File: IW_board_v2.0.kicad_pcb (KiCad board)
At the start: 2 copper layers, 167.8 x 92.4 mm, 104 parts, among them J1 USB_C_Receptacle, J10 RIGHT WHEEL SENS, J11 STARTER CON, J12 USB_C_Receptacle, J13 USB_C_Receptacle, J14 CAN, J15 3.3V OUT, J16 5V OUT, J17 7.5V OUT, J18 OIL CON, J19 IAT CON, J2 XT90PW-M, J20 PRIM TRIGG CON, J21 SEC TRIGG CON, J22 EGT CON, J23 DATA LOGGER CON, J24 IGN CON, J25 INJ CON, J3 EMU_BLACK_A, J4 EMU_BLACK_B, J5 SAFETY, J6 INJ CON, J7 STARTER INF, J8 SERVO, J9 LEFT WHEEL SENS, K1 FINDER-34.51 INJ, K2 FINDER-34.51 STARTER, K3 FINDER-34.51 INJ, Q1 IRFP1405PBF, Q2 IRFP1405PBF, Q3 IRFP1405PBF, Q4 IRFP1405PBF, SW1 TL3342F160QG/TR, SW2 TL3342F160QG/TR, U1 AP1501_3.3, U2 AP1501_5, U3 AP1501_ADJ_7.5, U4 RP2040, U5 LM4040DBZ-3, U6 W25Q32JVSS, U7 TXS0108EPWR, U8 2EDN7524F, Y1 Crystal

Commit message: First full version of the PCB
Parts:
- J10, J23, J24, J8, J9: footprint Connector_Molex:Molex_PicoBlade_53047-0310_1x03_P1.25mm_Vertical -> TerminalBlock_Phoenix:TerminalBlock_Phoenix_MPT-0,5-3-2.54_1x03_P2.54mm_Horizontal
- J14, J15, J16, J17, J18, J19, J20, J21, J22, J25, J5, J6, J7: footprint Connector_Molex:Molex_PicoBlade_53047-0210_1x02_P1.25mm_Vertical -> TerminalBlock_Phoenix:TerminalBlock_Phoenix_MPT-0,5-2-2.54_1x02_P2.54mm_Horizontal
- moved D6 124.3 mm to (63.0, 80.7)
- moved R10 124.3 mm to (63.0, 84.0), turned to 90 degrees
- moved D1 103.6 mm to (95.1, 92.4)
- moved L1 103.6 mm to (71.5, 85.8)
- moved C4 103.6 mm to (72.2, 100.2)
- moved C7 103.6 mm to (65.2, 104.1)
- moved U1 103.6 mm to (85.1, 98.1)
- moved C1 102.5 mm to (97.2, 101.7)
- moved D2 100.7 mm to (89.2, 88.5), turned to 0 degrees
- moved R2 97.4 mm to (174.2, 121.4), turned to 0 degrees
- moved R1 95.7 mm to (170.9, 121.4), turned to 0 degrees
- moved D4 95.0 mm to (175.0, 124.0), turned to 90 degrees
- moved C3 94.2 mm to (184.3, 138.2)
- moved L3 94.2 mm to (159.7, 122.2)
- moved C6 94.2 mm to (160.4, 136.5)
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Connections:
- net Net-(R3-Pad2) renamed /CPU/D+
- net Net-(R4-Pad2) renamed /CPU/D-
- J12 pad A1: Net-(J12-PadA1) -> /IO/USB_PASSTHROUH_GND
- J12 pad A12: Net-(J12-PadA1) -> /IO/USB_PASSTHROUH_GND
- J12 pad B1: Net-(J12-PadA1) -> /IO/USB_PASSTHROUH_GND
- J12 pad B12: Net-(J12-PadA1) -> /IO/USB_PASSTHROUH_GND
- J12 pad S1: Net-(J12-PadA1) -> /IO/USB_PASSTHROUH_GND
- R8 pad 2: /CPU/GPIO25 -> /CPU/GPIO11
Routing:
- net +5V: track 0.00 -> 336.5 mm, vias 0 -> 2
- net +3.3V: track 0.00 -> 309.7 mm, vias 0 -> 4
- net GNDS: track 0.00 -> 224.3 mm
- net /IO/RS232_TXD: track 0.00 -> 183.1 mm, vias 0 -> 2
- net /IO/5V EMU: track 0.00 -> 175.9 mm, vias 0 -> 2
- net Net-(J2-PadN): track 0.00 -> 161.2 mm
- net /IO/INJ: track 0.00 -> 158.5 mm, vias 0 -> 1
- net /IO/IGN: track 0.00 -> 154.8 mm, vias 0 -> 2
- net /IO/EMU: track 0.00 -> 153.9 mm, vias 0 -> 1
- net +7.5V: track 0.00 -> 149.8 mm, vias 0 -> 2
- net /IO/IGN_COIL_#1: track 0.00 -> 129.3 mm, vias 0 -> 2
- net /IO/EGT_IN_#1: track 0.00 -> 128.6 mm
- net /PWR/7.5V: track 0.00 -> 117.8 mm, vias 0 -> 2
- net VBUS: track 0.00 -> 111.4 mm, vias 0 -> 2
- net /IO/PRIM_TRIGG: track 0.00 -> 107.4 mm
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- added copper zone on B.Cu, net GND
- added copper zone on F.Cu, net GND
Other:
- board size 167.8 x 92.4 mm -> 155.8 x 92.4 mm

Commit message: Small corrections
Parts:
- added D11: B120-E3, Diode_SMD:D_SMA, F.Cu at (87.5, 110.1)
- added F9: 7.5V 5A, FUSE_3557-2:FUSE_3557-2, F.Cu at (110.2, 125.7)
- added J26: MAP, TerminalBlock_Phoenix:TerminalBlock_Phoenix_MPT-0,5-2-2.54_1x02_P2.54mm_Horizontal, F.Cu at (215.3, 90.5)
- added J27: CLT CON, TerminalBlock_Phoenix:TerminalBlock_Phoenix_MPT-0,5-2-2.54_1x02_P2.54mm_Horizontal, F.Cu at (147.6, 70.0)
- added R17: 330, Resistor_SMD:R_0603_1608Metric, F.Cu at (148.9, 75.3)
- D10, D9: value ES1J -> SS14; footprint ES1J:DIO_ES1J -> Diode_SMD:D_SMA
- D2, D3, D4: footprint Diode_SMD:D_0603_1608Metric -> Diode_SMD:D_SMA
- J3: footprint Connector_PinHeader_2.54mm:PinHeader_2x20_P2.54mm_Vertical -> Connector_IDC:IDC-Header_2x20_P2.54mm_Vertical
- J4: footprint Connector_PinHeader_2.54mm:PinHeader_2x12_P2.54mm_Vertical -> Connector_IDC:IDC-Header_2x12_P2.54mm_Vertical
- J6: value INJ CON -> INJ_&_STARTER
- J7: value STARTER INF -> 16V OUT
- R14: value 1k -> 10k
- moved K2 29.6 mm to (199.4, 110.0)
- moved K3 22.7 mm to (199.4, 87.0)
- moved D10 20.6 mm to (201.0, 103.0), turned to 180 degrees
- moved D4 18.8 mm to (193.8, 124.9), turned to 0 degrees
- moved J6 17.2 mm to (215.3, 98.5)
- moved J8 17.2 mm to (215.3, 109.1)
- moved J9 17.2 mm to (215.3, 119.6)
- moved J10 17.1 mm to (215.3, 130.1)
- moved J24 17.1 mm to (215.3, 140.7)
- moved J23 17.1 mm to (215.3, 151.2)
- moved R1 16.1 mm to (186.2, 126.5), turned to 180 degrees
- moved D9 15.7 mm to (201.0, 91.5), turned to 180 degrees
- moved J14 15.3 mm to (170.4, 70.0)
- moved J15 15.3 mm to (204.2, 70.0)
- moved J16 15.3 mm to (210.9, 70.0)
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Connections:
- C1 pad 1: VBUS -> Net-(C1-Pad1)
- C13 pad 1: /CPU/XOUT -> Net-(C13-Pad1)
- D1 pad 1: /PWR/3.3V -> Net-(C1-Pad1)
- J23 pad 1: /IO/5V EMU -> +5V
- J23 pad 3: GNDS -> GND
- J3 pad 20: /IO/VSS_IN -> /IO/RIGHT WHEEL OUT
- J5 pad 1: +BATT -> Net-(J5-Pad1)
- J5 pad 2: Net-(J5-Pad2) -> +BATT
- J6 pad 1: /IO/INJ IN -> Net-(D10-Pad1)
- J6 pad 2: /IO/INJ OUT -> /IO/INJ IN
- J7 pad 1: Net-(D10-PadK) -> GND
- J7 pad 2: Net-(D10-PadA) -> /PWR/16V
- K1 pad 11: /CPU/GPIO25 -> /CPU/GPIO21
- K1 pad A1: /IO/INJ IN -> GND
- K1 pad A2: /IO/INJ OUT -> /IO/INJ IN
- K2 pad 11: /CPU/GPIO24 -> /CPU/GPIO22
- K2 pad A1: Net-(D10-PadK) -> GND
- K2 pad A2: Net-(D10-PadA) -> Net-(D10-Pad1)
- K3 pad A1: /IO/INJ IN -> GND
- K3 pad A2: /IO/INJ OUT -> /IO/INJ IN
- Q1 pad 1: Net-(J5-Pad2) -> Net-(J5-Pad1)
- R13 pad 1: Net-(J5-Pad2) -> Net-(J5-Pad1)
- R14 pad 2: Net-(R14-Pad2) -> +3.3V
- R9 pad 1: /CPU/XOUT -> Net-(C13-Pad1)
- R9 pad 2: /CPU/XIN -> /CPU/XOUT
- U1 pad 1: /PWR/3.3V -> Net-(C1-Pad1)
- U7 pad 1: /CPU/GPIO21 -> /CPU/GPIO25
- U7 pad 10: Net-(R14-Pad2) -> +3.3V
- U7 pad 3: /CPU/GPIO22 -> /CPU/GPIO24
- U8 pad 2: /CPU/GPIO23 -> /CPU/GPIO10
- U8 pad 3: unconnected-(U8-Pad3) -> GND
- Y1 pad 1: /CPU/XOUT -> Net-(C13-Pad1)
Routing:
- net /IO/ANALOG_IN_#4: track 0.00 -> 164.8 mm, vias 0 -> 3
- net /IO/RIGHT WHEEL OUT: track 56.0 -> 202.1 mm, vias 1 -> 4
- net /PWR/16V: track 0.00 -> 134.7 mm, vias 0 -> 3
- net /IO/CLT_IN: track 0.00 -> 108.6 mm, vias 0 -> 1
- net Net-(J2-PadN): track 161.2 -> 77.8 mm
- net GNDS: track 224.3 -> 145.4 mm
- net /IO/IGN_COIL_#1: track 129.3 -> 205.1 mm, vias 2 -> 0
- net /IO/RS232_TXD: track 183.1 -> 249.0 mm, vias 2 -> 0
- net /IO/5V EMU: track 175.9 -> 113.4 mm
- net +5V: track 336.5 -> 388.1 mm
- net /CPU/GPIO24: track 65.4 -> 26.3 mm, vias 1 -> 2
- net /CPU/GPIO23: track 29.3 -> 0.00 mm, vias 2 -> 0
- net /IO/IGN: track 154.8 -> 183.8 mm, vias 2 -> 1
- net /IO/EGT_IN_#1: track 128.6 -> 156.3 mm
- net /IO/ANALOG_IN_#1: track 52.8 -> 80.2 mm
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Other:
- board size 155.8 x 92.4 mm -> 177.9 x 93.1 mm

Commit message: Added CAN transsiver to RP2040
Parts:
- removed U8: 2EDN7524F, 2EDN7524F:SOIC127P600X175-8N-22-V
- added C25: 100nF, Capacitor_SMD:C_0603_1608Metric, F.Cu at (157.7, 102.9)
- added C26: 10pF, Capacitor_SMD:C_0603_1608Metric, F.Cu at (149.5, 89.2)
- added C27: 10pF, Capacitor_SMD:C_0603_1608Metric, F.Cu at (143.5, 89.2)
- added C28: 100nF, Capacitor_SMD:C_0603_1608Metric, F.Cu at (168.7, 84.3)
- added J28: TPS CON, TerminalBlock_Phoenix:TerminalBlock_Phoenix_MPT-0,5-3-2.54_1x03_P2.54mm_Horizontal, F.Cu at (202.6, 149.6)
- added R18: 10k, Resistor_SMD:R_0603_1608Metric, F.Cu at (147.1, 106.0)
- added R19: 10k, Resistor_SMD:R_0603_1608Metric, F.Cu at (152.1, 107.5)
- added R20: 10k, Resistor_SMD:R_0603_1608Metric, F.Cu at (154.5, 105.5)
- added U10: SN65HVD232, Package_SO:SOIC-8_3.9x4.9mm_P1.27mm, F.Cu at (168.8, 79.4)
- added U9: MCP2515, Package_SO:SOIC-18W_7.5x11.6mm_P1.27mm, F.Cu at (149.7, 98.2)
- added Y2: Crystal, Crystal:Crystal_SMD_3225-4Pin_3.2x2.5mm, F.Cu at (146.5, 89.3)
- F9: value 7.5V 5A -> 16V 5A
- moved J27 2.59 mm to (150.2, 70.0), turned to 180 degrees
- moved SW2 1.89 mm to (150.7, 138.3)
- moved R17 1.11 mm to (147.8, 75.1), turned to -90 degrees
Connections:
- net /IO/CAN_H renamed CAN_H
- net /IO/CAN_L renamed CAN_L
- Q2 pad 1: Net-(Q2-Pad1) -> /IO/MOSFET_CONTROL
- Q3 pad 1: Net-(Q2-Pad1) -> /IO/MOSFET_CONTROL
- Q4 pad 1: Net-(Q2-Pad1) -> /IO/MOSFET_CONTROL
- U4 pad 27: /CPU/GPIO16 -> MISO
- U4 pad 28: /CPU/GPIO17 -> MCP2515_CS
- U4 pad 29: /CPU/GPIO18 -> SCK
- U4 pad 30: /CPU/GPIO19 -> MOSI
- U4 pad 39: /CPU/GPIO27 -> MCP2515_INT
- U7 pad 17: unconnected-(U7-Pad17) -> /IO/MOSFET_CONTROL
- U7 pad 4: unconnected-(U7-Pad4) -> /CPU/GPIO26
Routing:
- net /IO/TPS_IN: track 0.00 -> 232.2 mm, vias 0 -> 3
- net /IO/MOSFET_CONTROL: track 0.00 -> 97.7 mm, vias 0 -> 4
- net +5V: track 388.1 -> 328.9 mm, vias 2 -> 3
- net Net-(Q2-Pad1): track 56.3 -> 0.00 mm
- net MCP2515_CS: track 0.00 -> 53.0 mm, vias 0 -> 4
- net MISO: track 0.00 -> 50.6 mm, vias 0 -> 4
- net MOSI: track 0.00 -> 48.1 mm, vias 0 -> 4
- net SCK: track 0.00 -> 46.1 mm, vias 0 -> 4
- net +3.3V: track 304.8 -> 349.4 mm, vias 4 -> 7
- net /CPU/MCP2515/TXCAN: track 0.00 -> 32.5 mm
- net MCP2515_INT: track 0.00 -> 29.7 mm, vias 0 -> 2
- net /CPU/MCP2515/RXCAN: track 0.00 -> 25.5 mm
- net /CPU/GPIO26: track 0.00 -> 25.4 mm, vias 0 -> 4
- net /CPU/GPIO10: track 12.9 -> 0.00 mm
- net /CPU/MCP2515/MCP2515_OSC1: track 0.00 -> 5.59 mm
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
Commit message: Added lambda connection, switching between PWM and 3.3v signal to drive mosfets.
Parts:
- added C29: 1000uF, Capacitor_THT:CP_Radial_D8.0mm_P3.50mm, F.Cu at (92.8, 85.5)
- added J29: WBO CON, TerminalBlock_Phoenix:TerminalBlock_Phoenix_MPT-0,5-5-2.54_1x05_P2.54mm_Horizontal, F.Cu at (49.5, 78.4)
- added S1: JS102011SCQN, lib:SW_JS102011SCQN, F.Cu at (156.3, 123.5)
- moved R13 4.23 mm to (55.6, 100.1)
- moved Q1 4.13 mm to (49.9, 99.8)
- moved J5 1.96 mm to (50.7, 110.6)
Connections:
- U7 pad 4: /CPU/GPIO26 -> Net-(U7-Pad4)
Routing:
- net /IO/WBO_Heater: track 0.00 -> 138.4 mm, vias 0 -> 1
- net /IO/WBO_VGND: track 0.00 -> 55.2 mm, vias 0 -> 3
- net /IO/WBO_Ip: track 0.00 -> 37.5 mm, vias 0 -> 2
- net /IO/WBO_Rcal: track 0.00 -> 36.7 mm
- net +3.3V: track 349.4 -> 384.7 mm
- net /IO/WBO_Vs: track 0.00 -> 32.6 mm
- net /CPU/GPIO26: track 25.4 -> 47.2 mm, vias 4 -> 6
- net Net-(U7-Pad4): track 0.00 -> 12.7 mm
- net /IO/EMU: track 163.1 -> 158.3 mm
- net Net-(J2-PadN): track 77.8 -> 73.5 mm
- net /IO/CLT_IN: track 103.8 -> 99.7 mm
- net Net-(J5-Pad1): track 18.1 -> 14.8 mm
- net /CPU/GPIO22: track 50.9 -> 52.9 mm, vias 1 -> 2
- net +BATT: track 112.8 -> 111.2 mm
- net /IO/INJ_#1: track 70.2 -> 71.3 mm
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
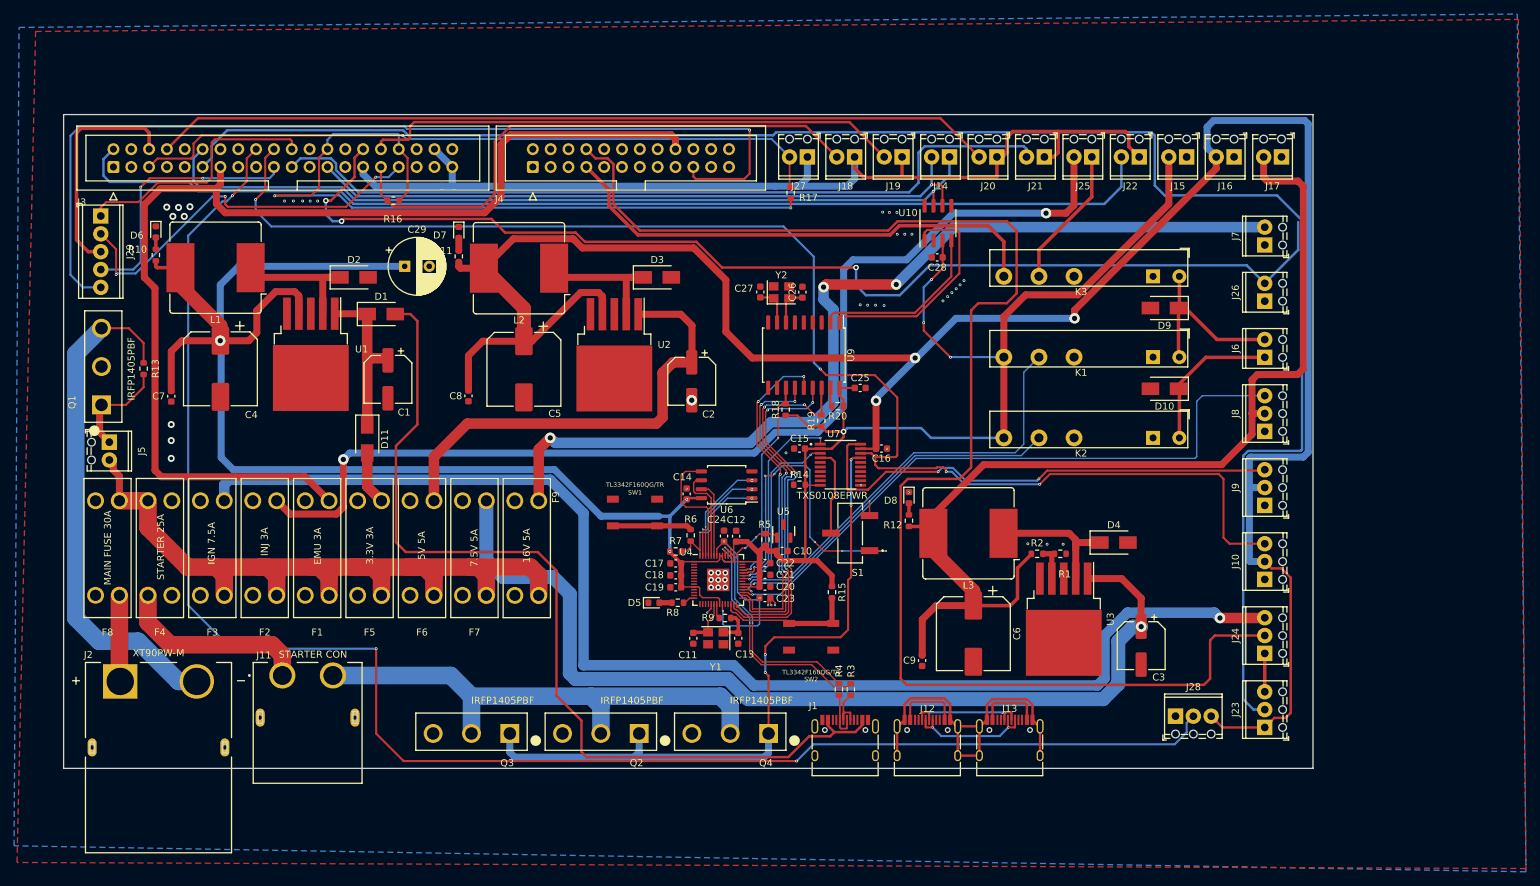
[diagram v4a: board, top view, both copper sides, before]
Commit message: Added DS1307 RTC and micro SD card
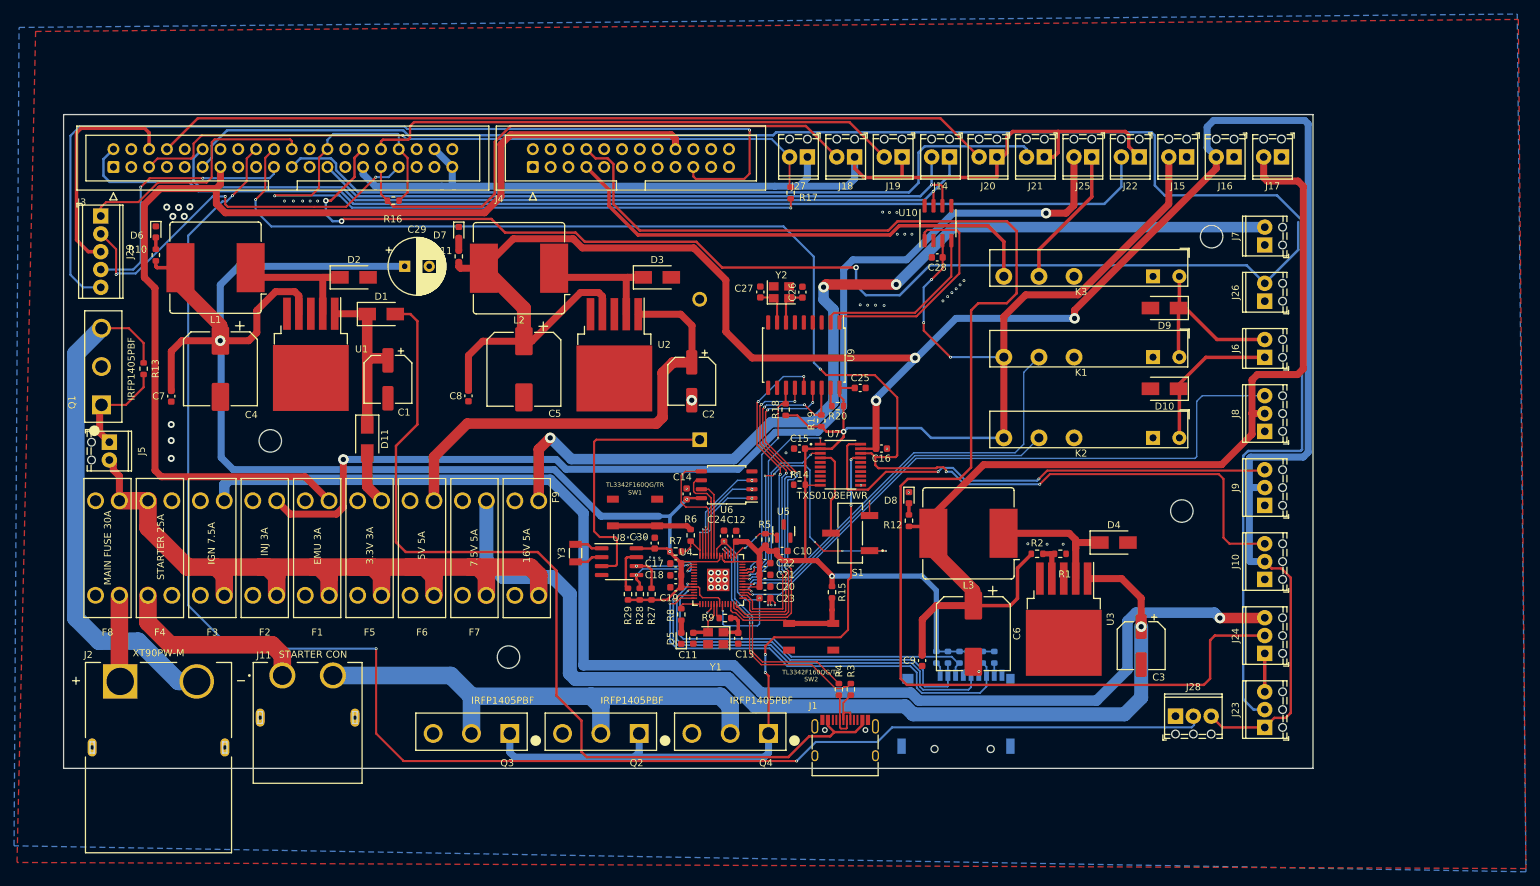
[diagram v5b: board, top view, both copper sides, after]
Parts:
- removed J12, J13: USB_C_Receptacle, Connector_USB:USB_C_Receptacle_HRO_TYPE-C-31-M-12
- added BT1: Battery_Cell, Battery:BatteryHolder_ComfortableElectronic_CH273-2450_1x2450, B.Cu at (134.8, 110.2)
- added C30: 0.1uF, Capacitor_SMD:C_0603_1608Metric, F.Cu at (128.4, 125.0)
- added J30: Micro_SD_Card, lib:112J-TDAR-R01, B.Cu at (176.3, 154.3)
- added R21: 3k3, Resistor_SMD:R_0603_1608Metric, B.Cu at (176.8, 141.2)
- added R22: 3k3, Resistor_SMD:R_0603_1608Metric, B.Cu at (175.1, 141.2)
- added R23: 3k3, Resistor_SMD:R_0603_1608Metric, B.Cu at (173.5, 141.2)
- added R24: 3k3, Resistor_SMD:R_0603_1608Metric, B.Cu at (171.8, 141.2)
- added R25: 3k3, Resistor_SMD:R_0603_1608Metric, B.Cu at (170.2, 141.2)
- added R26: 3k3, Resistor_SMD:R_0603_1608Metric, B.Cu at (168.5, 141.2)
- added R27: 4k7, Resistor_SMD:R_0603_1608Metric, F.Cu at (128.0, 132.2)
- added R28: 4k7, Resistor_SMD:R_0603_1608Metric, F.Cu at (126.3, 132.2)
- added R29: 4k7, Resistor_SMD:R_0603_1608Metric, F.Cu at (124.6, 132.2)
- added U8: DS1307+, Package_SO:SOIC-8_3.9x4.9mm_P1.27mm, F.Cu at (123.3, 127.6)
- added Y3: Crystal, Crystal:Crystal_SMD_3215-2Pin_3.2x1.5mm, F.Cu at (117.1, 126.4)
- moved D5 6.40 mm to (132.2, 138.5), turned to 90 degrees
- moved R8 1.74 mm to (132.2, 135.1), turned to 90 degrees
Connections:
- R8 pad 2: /CPU/GPIO11 -> /CPU/GPIO12
- U4 pad 11: /CPU/GPIO8 -> sd_card_miso
- U4 pad 13: /CPU/GPIO10 -> sd_card_sclk
- U4 pad 14: /CPU/GPIO11 -> sd_card_mosi
- U4 pad 2: /CPU/GPIO0 -> ds1307_sda
- U4 pad 3: /CPU/GPIO1 -> ds1307_scl
- U4 pad 9: /CPU/GPIO7 -> sd_card_cs
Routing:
- net sd_card_mosi: track 0.00 -> 62.5 mm, vias 0 -> 1
- net sd_card_sclk: track 0.00 -> 59.2 mm, vias 0 -> 1
- net sd_card_cs: track 0.00 -> 55.5 mm, vias 0 -> 1
- net /IO/USB_PASSTHROUH_GND: track 51.8 -> 0.00 mm
- net sd_card_miso: track 0.00 -> 51.2 mm, vias 0 -> 1
- net +3.3V: track 384.7 -> 434.9 mm, vias 7 -> 8
- net Net-(BT1-Pad1): track 0.00 -> 37.5 mm
- net /IO/USB_PASSTHROUH_VSYS: track 19.1 -> 0.00 mm
- net /IO/USB_PASSTHROUH_DP: track 18.1 -> 0.00 mm, vias 2 -> 0
- net /IO/USB_PASSTHROUH_DN: track 17.0 -> 0.00 mm, vias 2 -> 0
- net ds1307_scl: track 0.00 -> 15.9 mm, vias 0 -> 2
- net ds1307_sda: track 0.00 -> 10.9 mm, vias 0 -> 2
- net ds1307_sqw: track 0.00 -> 5.96 mm
- net /PWR/7.5V: track 137.3 -> 141.4 mm
- net GND: track 14.5 -> 10.4 mm, vias 51 -> 58
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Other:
- outline, holes or cut-outs redrawn

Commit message: Added 12V regulator for injector
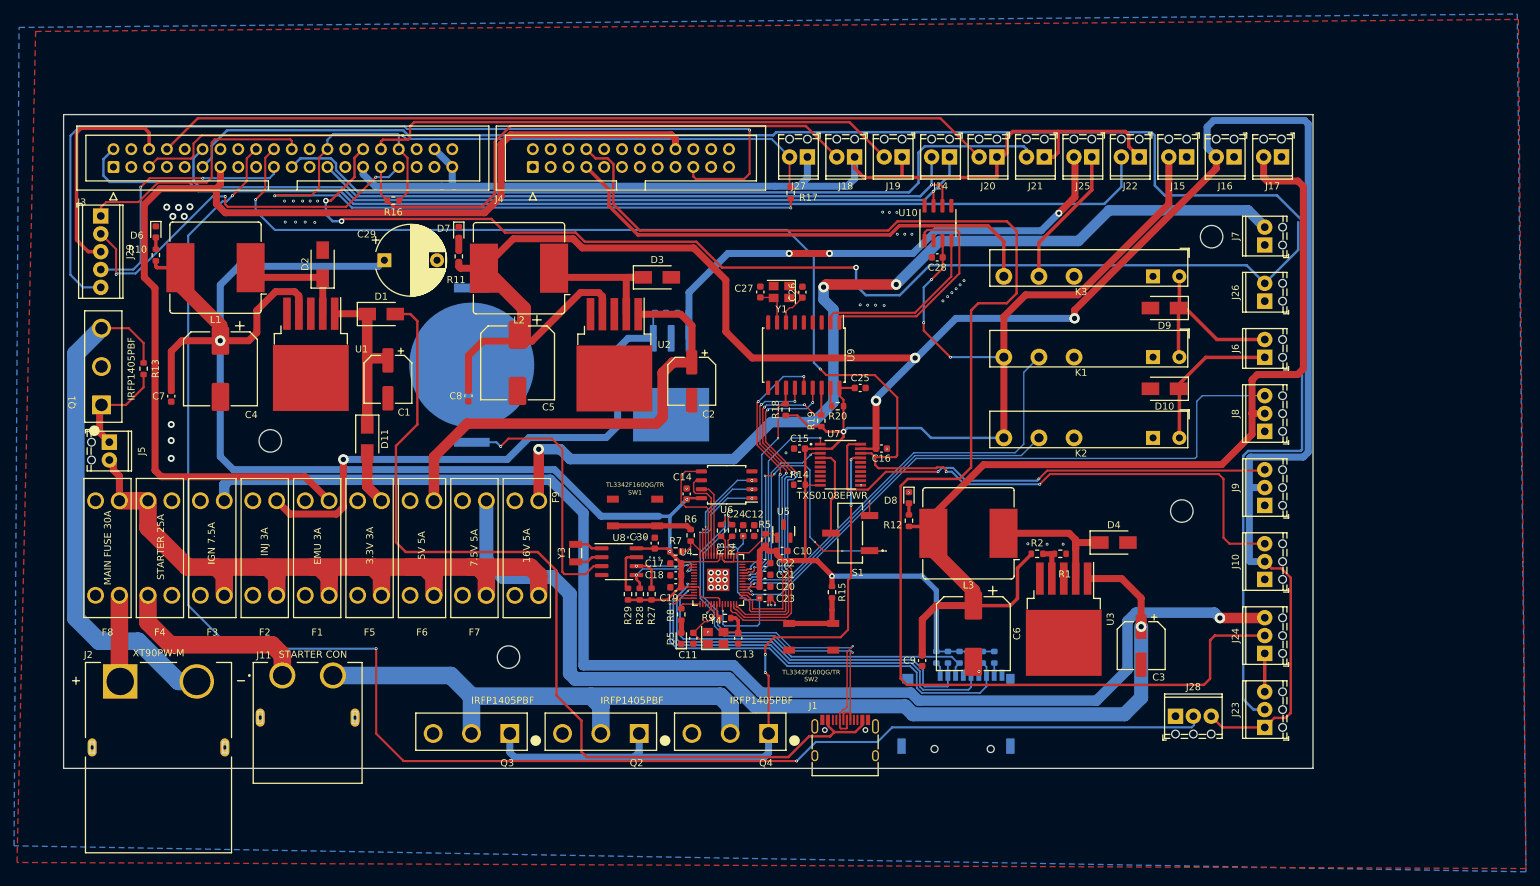
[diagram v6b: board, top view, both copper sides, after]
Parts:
- removed Y2: Crystal, Crystal:Crystal_SMD_3225-4Pin_3.2x2.5mm
- added C31: 0.1uF, Capacitor_SMD:C_0603_1608Metric, B.Cu at (132.4, 92.2)
- added C32: 0.22uF, Capacitor_SMD:C_0603_1608Metric, B.Cu at (129.2, 92.2)
- added U11: LM340S-12/NOPB, lib:TO254P1524X483-4N, B.Cu at (130.8, 102.2)
- added Y4: Crystal_GND24, Crystal:Crystal_SMD_3225-4Pin_3.2x2.5mm, F.Cu at (137.1, 138.5)
- BT1: footprint Battery:BatteryHolder_ComfortableElectronic_CH273-2450_1x2450 -> Battery:BatteryHolder_Keystone_3034_1x20mm
- C29: footprint Capacitor_THT:CP_Radial_D8.0mm_P3.50mm -> Capacitor_THT:CP_Radial_D10.0mm_P7.50mm
- Y1: value Crystal -> Crystal_GND24
- moved Y1 50.2 mm to (146.5, 89.2)
- moved BT1 34.2 mm to (102.4, 99.6)
- moved R3 29.2 mm to (137.9, 123.2), turned to -90 degrees
- moved R4 27.3 mm to (139.4, 123.2), turned to -90 degrees
- moved D2 4.85 mm to (81.1, 85.2), turned to 90 degrees
- moved C29 3.02 mm to (89.9, 84.7)
- moved C24 2.84 mm to (141.0, 123.2)
- moved C12 2.70 mm to (142.6, 123.2)
- moved C5 1.29 mm to (108.9, 99.3)
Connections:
- net /CPU/USB_DM renamed /CPU/USB_D-
- net /CPU/USB_DP renamed /CPU/USB_D+
- F2 pad 1: /IO/INJ -> /PWR/INJ
- J25 pad 2: /IO/INJ -> INJ_12V
- Y1 pad 1: Net-(C13-Pad1) -> /CPU/MCP2515/MCP2515_OSC2
- Y1 pad 2: /CPU/XIN -> GND
- Y1 pad 3: (no net) -> /CPU/MCP2515/MCP2515_OSC1
- Y1 pad 4: (no net) -> GND
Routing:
- net /IO/INJ: track 156.1 -> 0.00 mm, vias 2 -> 0
- net /PWR/INJ: track 0.00 -> 78.9 mm, vias 0 -> 1
- net INJ_12V: track 0.00 -> 73.0 mm, vias 0 -> 3
- net /CPU/USB_D-: track 6.92 -> 57.2 mm, vias 0 -> 2
- net /CPU/USB_D+: track 6.95 -> 52.8 mm, vias 0 -> 2
- net /CPU/D+: track 34.2 -> 3.02 mm, vias 2 -> 0
- net /CPU/D-: track 32.1 -> 3.01 mm, vias 2 -> 0
- net +3.3V: track 434.9 -> 426.2 mm
- net Net-(D2-K): track 20.9 -> 16.1 mm
- net /CPU/XIN: track 6.51 -> 8.47 mm
- net /CPU/MCP2515/MCP2515_OSC2: track 5.56 -> 7.32 mm
- net +1V1: track 28.6 -> 29.6 mm, vias 3 -> 5
- net Net-(BT1-+): track 37.5 -> 38.0 mm, vias 0 -> 1
- net Net-(U4-ADC_AVDD): track 7.45 -> 7.67 mm, vias 2 -> 0
- net GND: vias 58 -> 63
